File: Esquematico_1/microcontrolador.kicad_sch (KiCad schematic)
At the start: 33 parts, among them U2 STM32F405RGTx

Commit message: Update Footprint sw reset
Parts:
- SwReset1: footprint (none) -> Button_Switch_SMD:SW_SPST_Omron_B3FS-100xP
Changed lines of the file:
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@@
 			)
 		)
-		(property "Footprint" ""
+		(property "Footprint" "Button_Switch_SMD:SW_SPST_Omron_B3FS-100xP"
 			(at 91.44 167.64 0)
 			(effects

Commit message: Update footprint sw rst
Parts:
- SwReset1: footprint Button_Switch_SMD:SW_SPST_Omron_B3FS-100xP -> Button_Switch_SMD:SW_Push_SPST_NO_Alps_SKRK
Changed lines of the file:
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@@
 			)
 		)
-		(property "Footprint" "Button_Switch_SMD:SW_SPST_Omron_B3FS-100xP"
+		(property "Footprint" "Button_Switch_SMD:SW_Push_SPST_NO_Alps_SKRK"
 			(at 91.44 167.64 0)
 			(effects

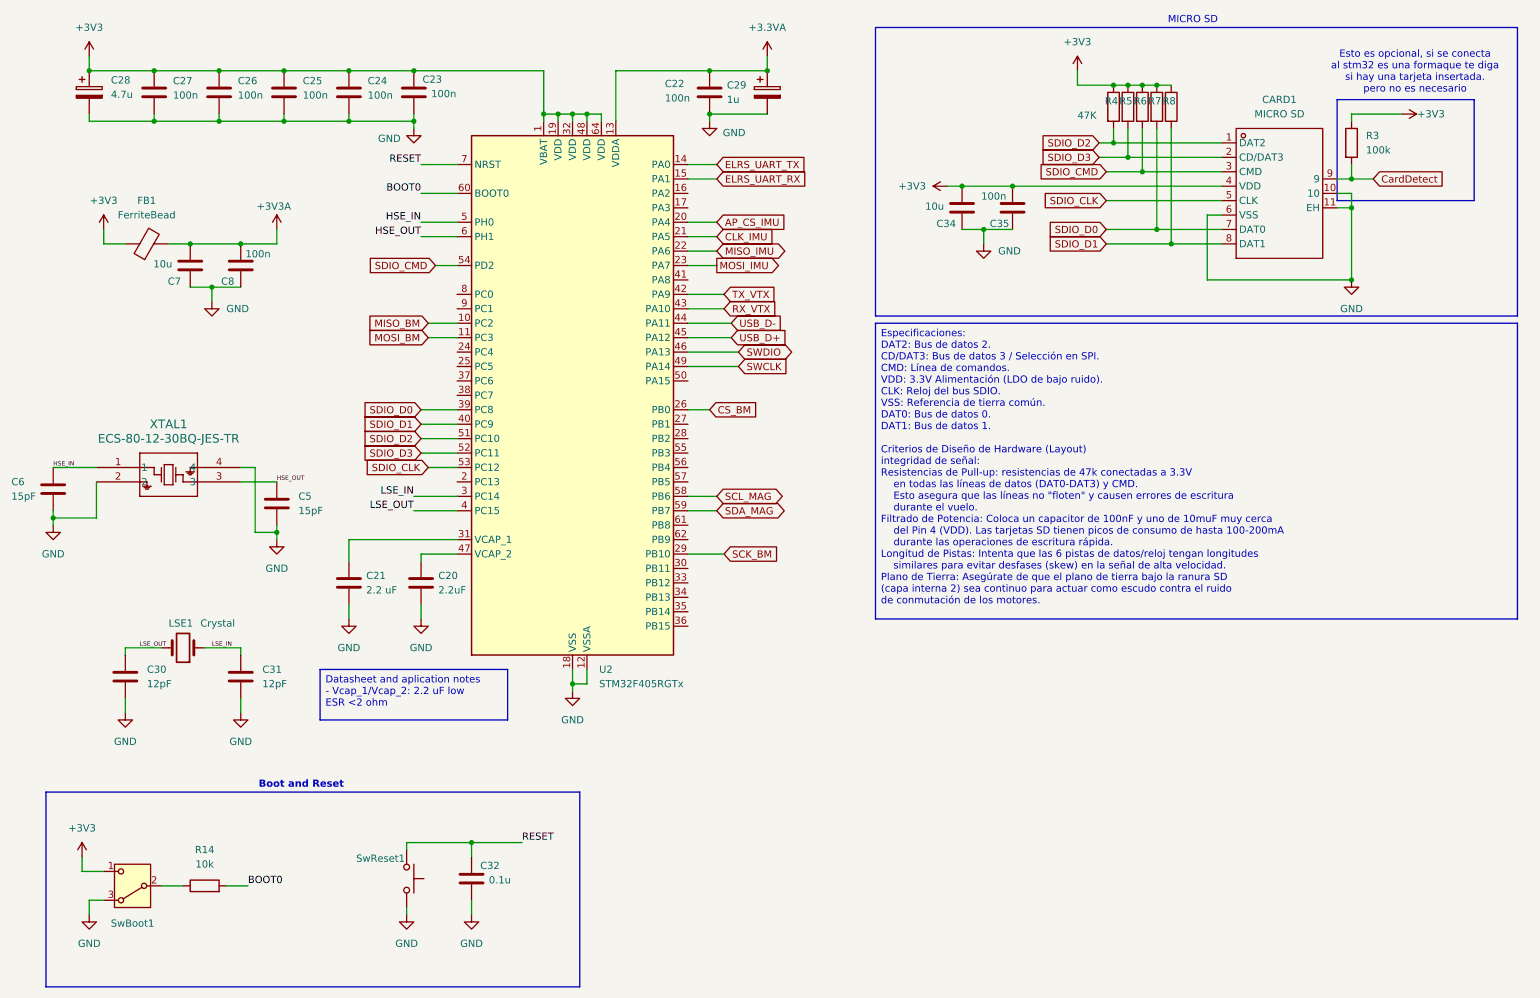
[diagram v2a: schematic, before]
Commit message: LDS y gran corrección de errores del esquemático
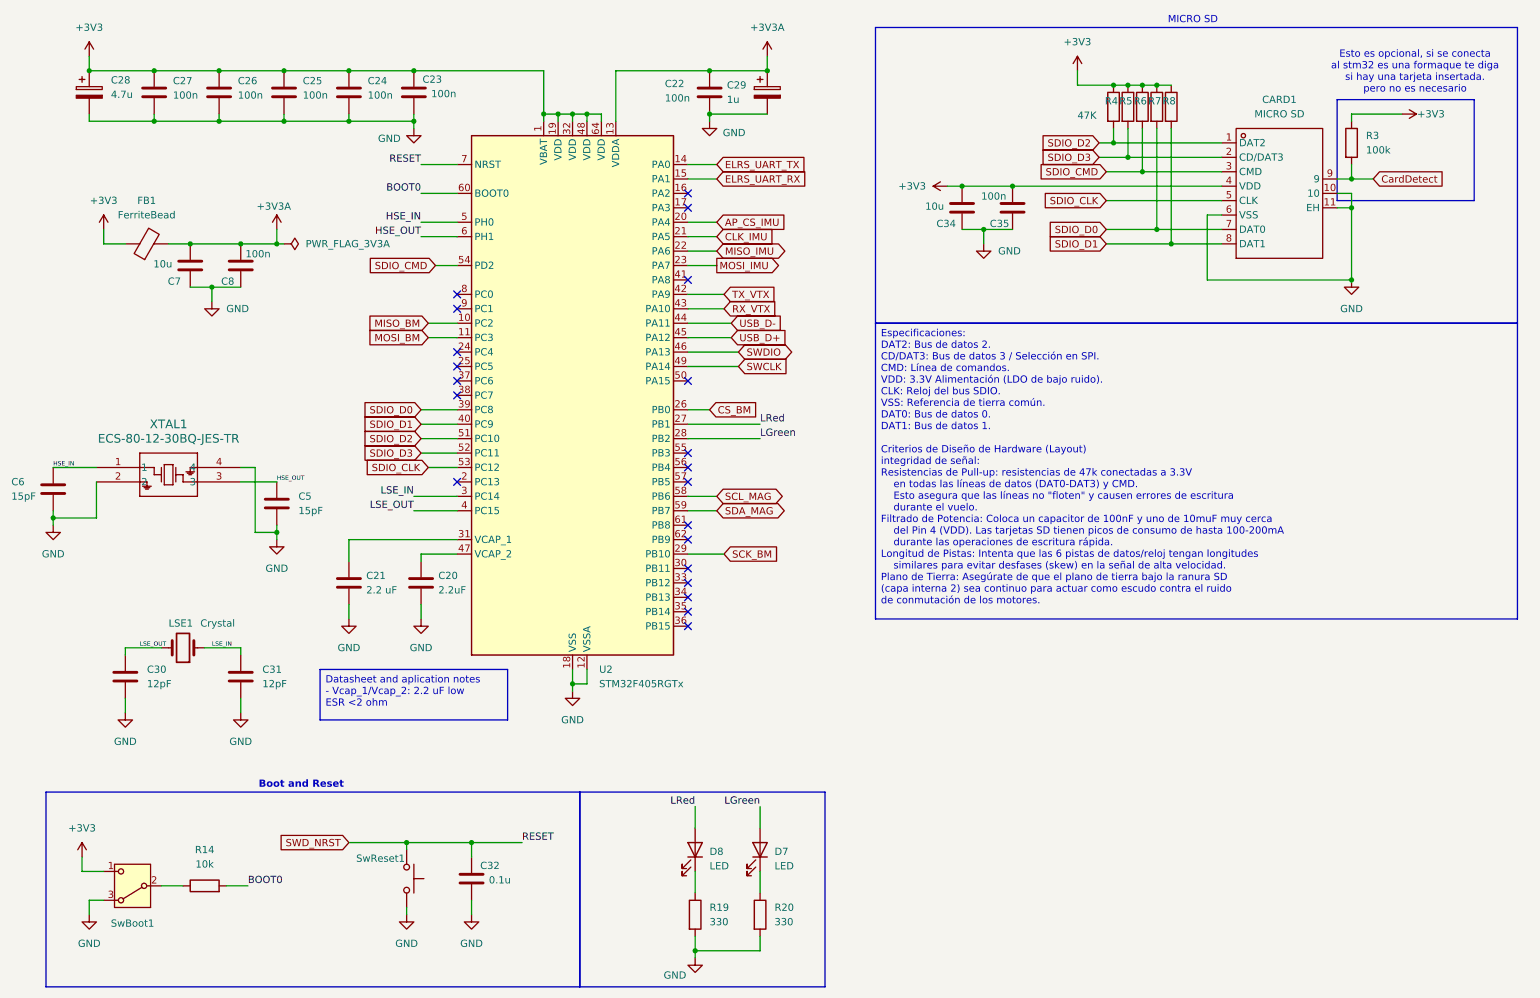
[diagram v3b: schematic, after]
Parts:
- added D7, D8: LED, symbol Device:LED
- added R19, R20: 330, Resistor_SMD:R_0805_2012Metric_Pad1.20x1.40mm_HandSolder, symbol Device:R
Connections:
- net +3.3VA is gone; now on net +3V3A: C22.1, C29.1, U2.13 (VDDA)
- net GND: now also R19.2, R20.2
- net LRed: now reaches U2.27 (PB1)
- net LRed: now also D8.2 (A)
- net LGreen: now reaches U2.28 (PB2)
- net LGreen: now also D7.2 (A)
- net RESET renamed SWD_NRST
- new net: D7.1 (K), R20.1
- new net: D8.1 (K), R19.1
- no-connect marks 0 -> 21

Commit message: Todos los footprints menos ESC
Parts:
- D7, D8: footprint (none) -> LED_SMD:LED_0805_2012Metric_Pad1.15x1.40mm_HandSolder
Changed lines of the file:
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@@
 			)
 		)
-		(property "Footprint" ""
+		(property "Footprint" "LED_SMD:LED_0805_2012Metric_Pad1.15x1.40mm_HandSolder"
 			(at 148.59 162.56 0)
 			(effects
@@
 			)
 		)
-		(property "Footprint" ""
+		(property "Footprint" "LED_SMD:LED_0805_2012Metric_Pad1.15x1.40mm_HandSolder"
 			(at 137.16 162.56 0)
 			(effects

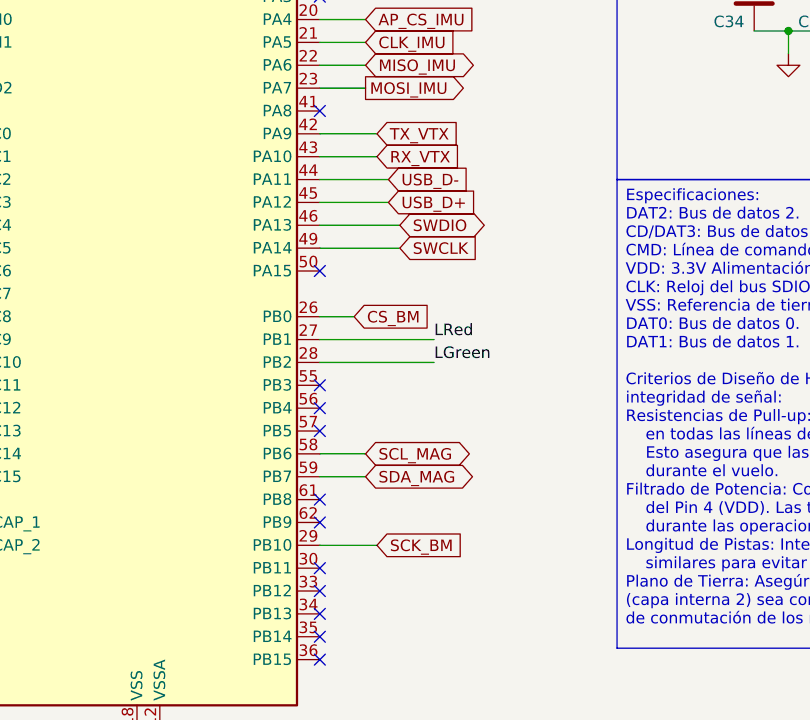
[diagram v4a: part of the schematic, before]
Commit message: Cambios netclasses, rules en el PCB, conección de los cristales
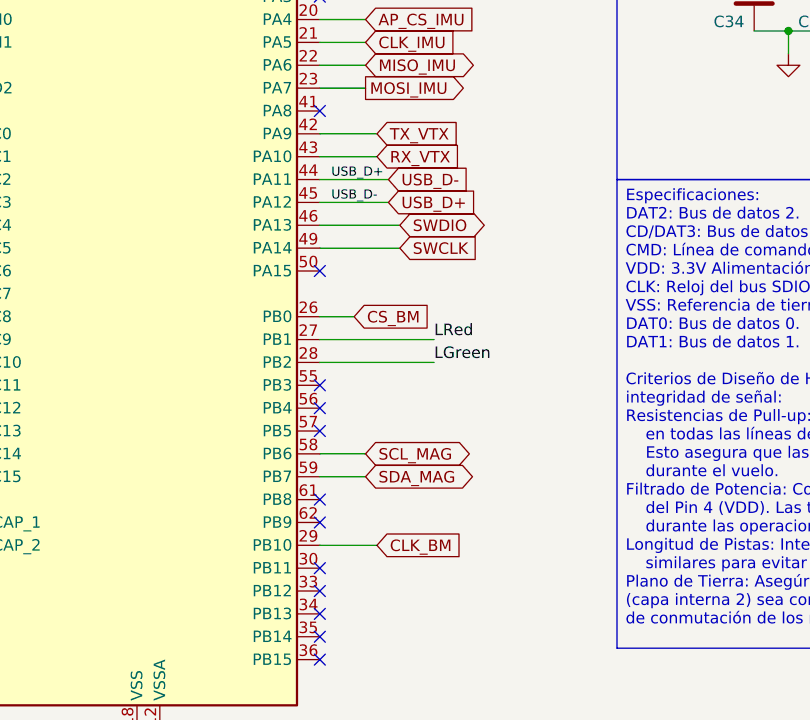
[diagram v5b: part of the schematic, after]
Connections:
- net USB_D- is gone; now on net USB_D+: U2.44 (PA11)
- net SCK_BM renamed CLK_BM
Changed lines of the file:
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@@
+		)
+	)
+	(label "USB_D-"
+		(at 137.16 72.39 0)
+		(effects
+			(font
+				(size 1.016 1.016)
+			)
+			(justify left bottom)
 		)
 	)
@@
 			)
 			(justify right bottom)
+		)
+	)
+	(label "USB_D+"
+		(at 137.16 69.85 0)
+		(effects
+			(font
+				(size 1.016 1.016)
+			)
+			(justify left bottom)
 		)
 	)
@@
 		)
 	)
-	(global_label "SCK_BM"
+	(global_label "CLK_BM"
 		(shape input)
 		(at 142.24 110.49 0)
@@
 		)
 		(property "Intersheetrefs" "${INTERSHEET_REFS}"
-			(at 152.6637 110.49 0)
+			(at 152.4823 110.49 0)
 			(effects
 				(font

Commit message: BIG Update conexionado MCU y PCB
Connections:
- net AP_CS_IMU: now also U2.25 (PC5); no longer U2.20 (PA4)
- net CLK_BM: now also U2.34 (PB13); no longer U2.29 (PB10)
- net CS_BM: now also U2.33 (PB12); no longer U2.26 (PB0)
- net CardDetect: now also U2.56 (PB4)
- net MISO_BM: now also U2.35 (PB14); no longer U2.10 (PC2)
- net MOSI_BM: now also U2.36 (PB15); no longer U2.11 (PC3)
- net USB_D+: no longer U2.44 (PA11)
- net ESC3: now reaches U2.16 (PA2)
- net ESC4: now reaches U2.17 (PA3)
- net CRT: now reaches U2.24 (PC4)
- net GPS_UART_RX: now reaches U2.30 (PB11)
- net TELEM_ESC: now reaches U2.38 (PC7)
- net ESC1: now reaches U2.50 (PA15)
- net ESC2: now reaches U2.55 (PB3)
- net INT_BM: now reaches U2.9 (PC1)
- new net GPS_UART_TX: U2.29 (PB10)
- new net INT1_IMU: U2.10 (PC2)
- new net INT2_IMU: U2.11 (PC3)
- new net USB_D-: U2.44 (PA11)
- no-connect marks 21 -> 9

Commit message: Cristal corregido
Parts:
- C22, C25, C27, C32: footprint Capacitor_SMD:C_0805_2012Metric_Pad1.18x1.45mm_HandSolder -> Capacitor_SMD:C_0603_1608Metric_Pad1.08x0.95mm_HandSolder
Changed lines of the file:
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@@
 			)
 		)
-		(property "Footprint" "Capacitor_SMD:C_0805_2012Metric_Pad1.18x1.45mm_HandSolder"
+		(property "Footprint" "Capacitor_SMD:C_0603_1608Metric_Pad1.08x0.95mm_HandSolder"
 			(at 98.7552 171.45 0)
 			(effects
@@
 			)
 		)
-		(property "Footprint" "Capacitor_SMD:C_0805_2012Metric_Pad1.18x1.45mm_HandSolder"
+		(property "Footprint" "Capacitor_SMD:C_0603_1608Metric_Pad1.08x0.95mm_HandSolder"
 			(at 65.7352 33.02 0)
 			(effects
@@
 			)
 		)
-		(property "Footprint" "Capacitor_SMD:C_0805_2012Metric_Pad1.18x1.45mm_HandSolder"
+		(property "Footprint" "Capacitor_SMD:C_0603_1608Metric_Pad1.08x0.95mm_HandSolder"
 			(at 140.6652 33.02 0)
 			(effects
@@
 			)
 		)
-		(property "Footprint" "Capacitor_SMD:C_0805_2012Metric_Pad1.18x1.45mm_HandSolder"
+		(property "Footprint" "Capacitor_SMD:C_0603_1608Metric_Pad1.08x0.95mm_HandSolder"
 			(at 42.8752 33.02 0)
 			(effects

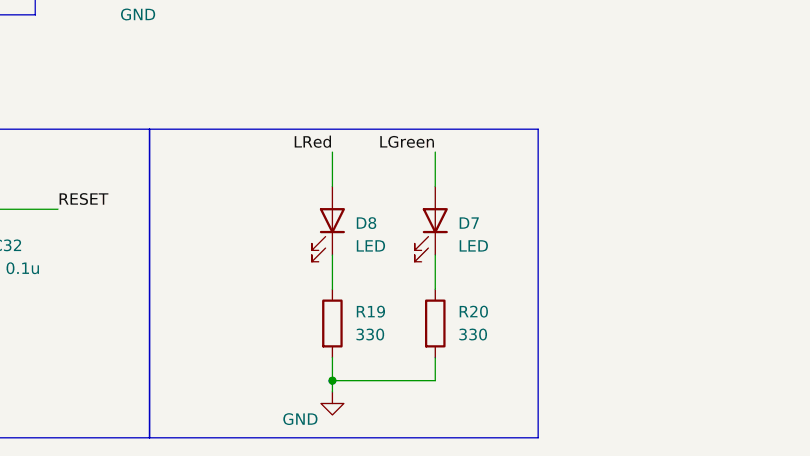
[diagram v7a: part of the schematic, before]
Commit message: Magnometro listo y luces led
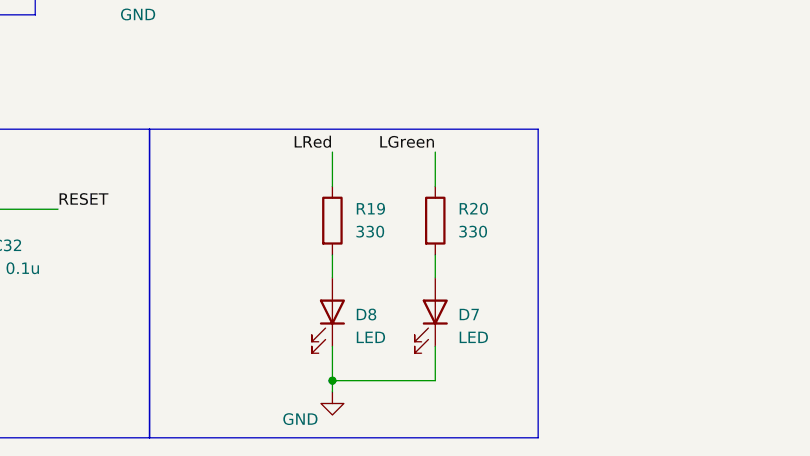
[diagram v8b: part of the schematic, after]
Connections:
- net GND: now also D7.1 (K), D8.1 (K); no longer R19.2, R20.2
- net LGreen: now also R20.1; no longer D7.2 (A)
- net LRed: now also R19.1; no longer D8.2 (A)
- new net: D7.2 (A), R20.2
- new net: D8.2 (A), R19.2
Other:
- moved on the sheet: D7, D8, R19, R20
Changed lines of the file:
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@@
 	(wire
 		(pts
+			(xy 137.16 166.37) (xy 137.16 168.91)
+		)
+		(stroke
+			(width 0)
+			(type default)
+		)
+	)
+	(wire
+		(pts
 			(xy 76.2 119.38) (xy 76.2 121.92)
 		)
@@
 	(wire
 		(pts
-			(xy 137.16 166.37) (xy 137.16 170.18)
-		)
-		(stroke
-			(width 0)
-			(type default)
-		)
-	)
-	(wire
-		(pts
 			(xy 95.25 85.09) (xy 88.9 85.09)
 		)
@@
 	(wire
 		(pts
+			(xy 137.16 154.94) (xy 137.16 158.75)
+		)
+		(stroke
+			(width 0)
+			(type default)
+		)
+	)
+	(wire
+		(pts
 			(xy 48.26 55.88) (xy 57.15 55.88)
 		)
@@
 	(wire
 		(pts
+			(xy 148.59 166.37) (xy 148.59 168.91)
+		)
+		(stroke
+			(width 0)
+			(type default)
+		)
+	)
+	(wire
+		(pts
 			(xy 140.97 92.71) (xy 135.89 92.71)
 		)
@@
 	(wire
 		(pts
-			(xy 137.16 154.94) (xy 137.16 158.75)
-		)
-		(stroke
-			(width 0)
-			(type default)
-		)
-	)
-	(wire
-		(pts
 			(xy 76.2 33.02) (xy 76.2 34.29)
 		)
@@
 	(wire
 		(pts
-			(xy 33.02 53.34) (xy 33.02 55.88)
+			(xy 137.16 176.53) (xy 137.16 180.34)
 		)
 		(stroke
@@
 	(wire
 		(pts
-			(xy 88.9 77.47) (xy 95.25 77.47)
+			(xy 33.02 53.34) (xy 33.02 55.88)
 		)
 		(stroke
@@
 	(wire
 		(pts
-			(xy 88.9 87.63) (xy 95.25 87.63)
+			(xy 88.9 77.47) (xy 95.25 77.47)
 		)
 		(stroke
@@
 	(wire
 		(pts
-			(xy 52.07 63.5) (xy 57.15 63.5)
+			(xy 88.9 87.63) (xy 95.25 87.63)
 		)
 		(stroke
@@
 	(wire
 		(pts
-			(xy 252.73 33.02) (xy 252.73 34.29)
+			(xy 52.07 63.5) (xy 57.15 63.5)
 		)
 		(stroke
@@
 	(wire
 		(pts
-			(xy 137.16 177.8) (xy 137.16 180.34)
+			(xy 252.73 33.02) (xy 252.73 34.29)
 		)
 		(stroke
@@
 	(wire
 		(pts
-			(xy 148.59 154.94) (xy 148.59 158.75)
+			(xy 135.89 123.19) (xy 142.24 123.19)
 		)
 		(stroke
@@
 	(wire
 		(pts
-			(xy 135.89 123.19) (xy 142.24 123.19)
+			(xy 252.73 49.53) (xy 252.73 62.23)
 		)
 		(stroke
@@
 	(wire
 		(pts
-			(xy 252.73 49.53) (xy 252.73 62.23)
+			(xy 213.36 27.94) (xy 215.9 27.94)
 		)
 		(stroke
@@
 	(wire
 		(pts
-			(xy 213.36 27.94) (xy 215.9 27.94)
+			(xy 148.59 154.94) (xy 148.59 158.75)
 		)
 		(stroke
@@
 	(wire
 		(pts
-			(xy 148.59 177.8) (xy 148.59 180.34)
+			(xy 148.59 176.53) (xy 148.59 180.34)
 		)
 		(stroke
@@
 	(wire
 		(pts
-			(xy 148.59 166.37) (xy 148.59 170.18)
-		)
-		(stroke
-			(width 0)
-			(type default)
-		)
-	)
-	(wire
-		(pts
 			(xy 215.9 27.94) (xy 218.44 27.94)
 		)
@@
 	(symbol
 		(lib_id "Device:LED")
-		(at 148.59 162.56 270)
+		(at 148.59 172.72 270)
 		(mirror x)
 		(unit 1)
@@
 		(fields_autoplaced yes)
 		(property "Reference" "D7"
-			(at 151.13 162.8774 90)
+			(at 151.13 173.0374 90)
 			(effects
 				(font
@@
 		)
 		(property "Value" "LED"
-			(at 151.13 165.4174 90)
+			(at 151.13 175.5774 90)
 			(effects
 				(font
@@
 		)
 		(property "Footprint" "LED_SMD:LED_0805_2012Metric_Pad1.15x1.40mm_HandSolder"
-			(at 148.59 162.56 0)
+			(at 148.59 172.72 0)
 			(effects
 				(font
@@
 		)
 		(property "Datasheet" "~"
-			(at 148.59 162.56 0)
+			(at 148.59 172.72 0)
 			(effects
 				(font
@@
 		)
 		(property "Description" "Light emitting diode"
-			(at 148.59 162.56 0)
+			(at 148.59 172.72 0)
 			(effects
 				(font
@@
 		)
 		(property "Sim.Pins" "1=K 2=A"
-			(at 148.59 162.56 0)
+			(at 148.59 172.72 0)
 			(effects
 				(font
@@
 	(symbol
 		(lib_id "Device:R")
-		(at 148.59 173.99 0)
+		(at 148.59 162.56 0)
 		(unit 1)
 		(exclude_from_sim no)
@@
 		(fields_autoplaced yes)
 		(property "Reference" "R20"
-			(at 151.13 172.7199 0)
+			(at 151.13 161.2899 0)
 			(effects
 				(font
@@
 		)
 		(property "Value" "330"
-			(at 151.13 175.2599 0)
+			(at 151.13 163.8299 0)
 			(effects
 				(font
@@
 		)
 		(property "Footprint" "Resistor_SMD:R_0805_2012Metric_Pad1.20x1.40mm_HandSolder"
-			(at 146.812 173.99 90)
+			(at 146.812 162.56 90)
 			(effects
 				(font
@@
 		)
 		(property "Datasheet" "~"
-			(at 148.59 173.99 0)
+			(at 148.59 162.56 0)
 			(effects
 				(font
@@
 		)
 		(property "Description" "Resistor"
-			(at 148.59 173.99 0)
+			(at 148.59 162.56 0)
 			(effects
 				(font
@@
 	(symbol
 		(lib_id "Device:R")
-		(at 137.16 173.99 0)
+		(at 137.16 162.56 0)
 		(unit 1)
 		(exclude_from_sim no)
@@
 		(fields_autoplaced yes)
 		(property "Reference" "R19"
-			(at 139.7 172.7199 0)
+			(at 139.7 161.2899 0)
 			(effects
 				(font
@@
 		)
 		(property "Value" "330"
-			(at 139.7 175.2599 0)
+			(at 139.7 163.8299 0)
 			(effects
 				(font
@@
 		)
 		(property "Footprint" "Resistor_SMD:R_0805_2012Metric_Pad1.20x1.40mm_HandSolder"
-			(at 135.382 173.99 90)
+			(at 135.382 162.56 90)
 			(effects
 				(font
@@
 		)
 		(property "Datasheet" "~"
-			(at 137.16 173.99 0)
+			(at 137.16 162.56 0)
 			(effects
 				(font
@@
 		)
 		(property "Description" "Resistor"
-			(at 137.16 173.99 0)
+			(at 137.16 162.56 0)
 			(effects
 				(font
@@
 		)
 		(instances
-			(project ""
+			(project "Esquematico_1"
 				(path "/de2d80c1-c21c-478d-b724-17659b714c38/65191e46-6d87-4ab8-a02b-a5dd631b354a"
 					(reference "R19")
@@
 	(symbol
 		(lib_id "Device:LED")
-		(at 137.16 162.56 270)
+		(at 137.16 172.72 270)
 		(mirror x)
 		(unit 1)
@@
 		(fields_autoplaced yes)
 		(property "Reference" "D8"
-			(at 139.7 162.8774 90)
+			(at 139.7 173.0374 90)
 			(effects
 				(font
@@
 		)
 		(property "Value" "LED"
-			(at 139.7 165.4174 90)
+			(at 139.7 175.5774 90)
 			(effects
 				(font
@@
 		)
 		(property "Footprint" "LED_SMD:LED_0805_2012Metric_Pad1.15x1.40mm_HandSolder"
-			(at 137.16 162.56 0)
+			(at 137.16 172.72 0)
 			(effects
 				(font
@@
 		)
 		(property "Datasheet" "~"
-			(at 137.16 162.56 0)
+			(at 137.16 172.72 0)
 			(effects
 				(font
@@
 		)
 		(property "Description" "Light emitting diode"
-			(at 137.16 162.56 0)
+			(at 137.16 172.72 0)
 			(effects
 				(font
@@
 		)
 		(property "Sim.Pins" "1=K 2=A"
-			(at 137.16 162.56 0)
+			(at 137.16 172.72 0)
 			(effects
 				(font
